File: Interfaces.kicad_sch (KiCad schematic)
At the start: 13 parts, among them J10 UART1_HDR, J11 UART2_HDR, J13 I2C1_Headers, J4 I/O_HDR, U8 TCA9517D

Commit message: Interface Update
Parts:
- removed FPC5, FPC6: FPC_0545481072, Personal_Project:FPC_10051922_1010, symbol Personal_Projects:FPC_0545481072
- removed J10: UART1_HDR, Personal_Project:PinHeader_2x03_P2.54mm_Horizontal_Court, symbol Connector_Generic:Conn_02x03_Odd_Even
- removed J11: UART2_HDR, Personal_Project:PinHeader_2x03_P2.54mm_Horizontal_Court, symbol Connector_Generic:Conn_02x03_Odd_Even
- removed J4: I/O_HDR, Connector_PinHeader_2.54mm:PinHeader_2x05_P2.54mm_Horizontal, symbol Connector_Generic:Conn_02x05_Odd_Even
- removed R16, R23: 33R, Resistor_SMD:R_0805_2012Metric, symbol Device:R
- removed U8: TCA9517D, Package_SO:SOIC-8_3.9x4.9mm_P1.27mm, symbol Logic_LevelTranslator:TCA9517D
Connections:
- net SCLB is gone; now on net I2C_SCL_HDR: DI2.1 (K1), J13.5 (Pin_5)
- net SDAB is gone; now on net I2C_SDA_HDR: DI2.2 (K2), J13.1 (Pin_1)
- net GND: no longer J13.2 (Pin_2), J13.6 (Pin_6)
- new net UART0_RXD: J13.6 (Pin_6)
- new net UART0_TXD: J13.2 (Pin_2)
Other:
- company: (none) -> Peter Hancak
- title: (none) -> ESP32P4C5_BOARD
- moved on the sheet: DI2, FPC1, J13, R30, R31

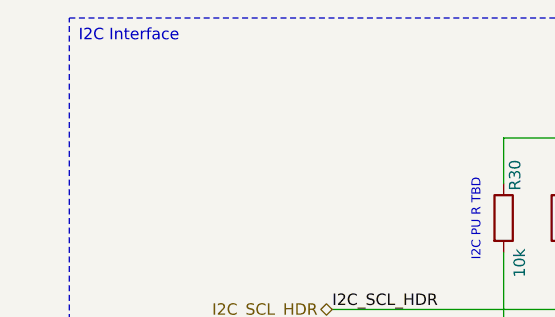
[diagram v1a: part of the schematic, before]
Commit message: Small trace layout fixes
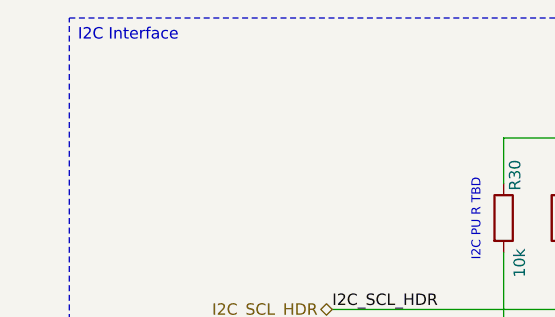
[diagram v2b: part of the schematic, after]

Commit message: Power rail update
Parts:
- added RN17: 22R, Resistor_SMD:R_Array_Convex_4x0402, symbol Device:R_Pack04
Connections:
- net SPI_CLK: now also RN17.7 (R2.2)
- net SPI_CS: now also RN17.8 (R1.2)
- net SPI_MISO: now also RN17.6 (R3.2)
- net SPI_MOSI: now also RN17.5 (R4.2)
- new net SPI_0_CLK_R: RN17.2 (R2.1)
- new net SPI_0_CS_R: RN17.1 (R1.1)
- new net SPI_0_MISO_R: RN17.3 (R3.1)
- new net SPI_0_MOSI_R: RN17.4 (R4.1)
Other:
- note added: "Series Reflection Attenuation R TBD"
- moved on the sheet: DI2, FPC1, J13, R30, R31
